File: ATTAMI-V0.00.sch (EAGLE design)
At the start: 23 parts, among them U1 MIC5225, U2 ATTINY85-20SU

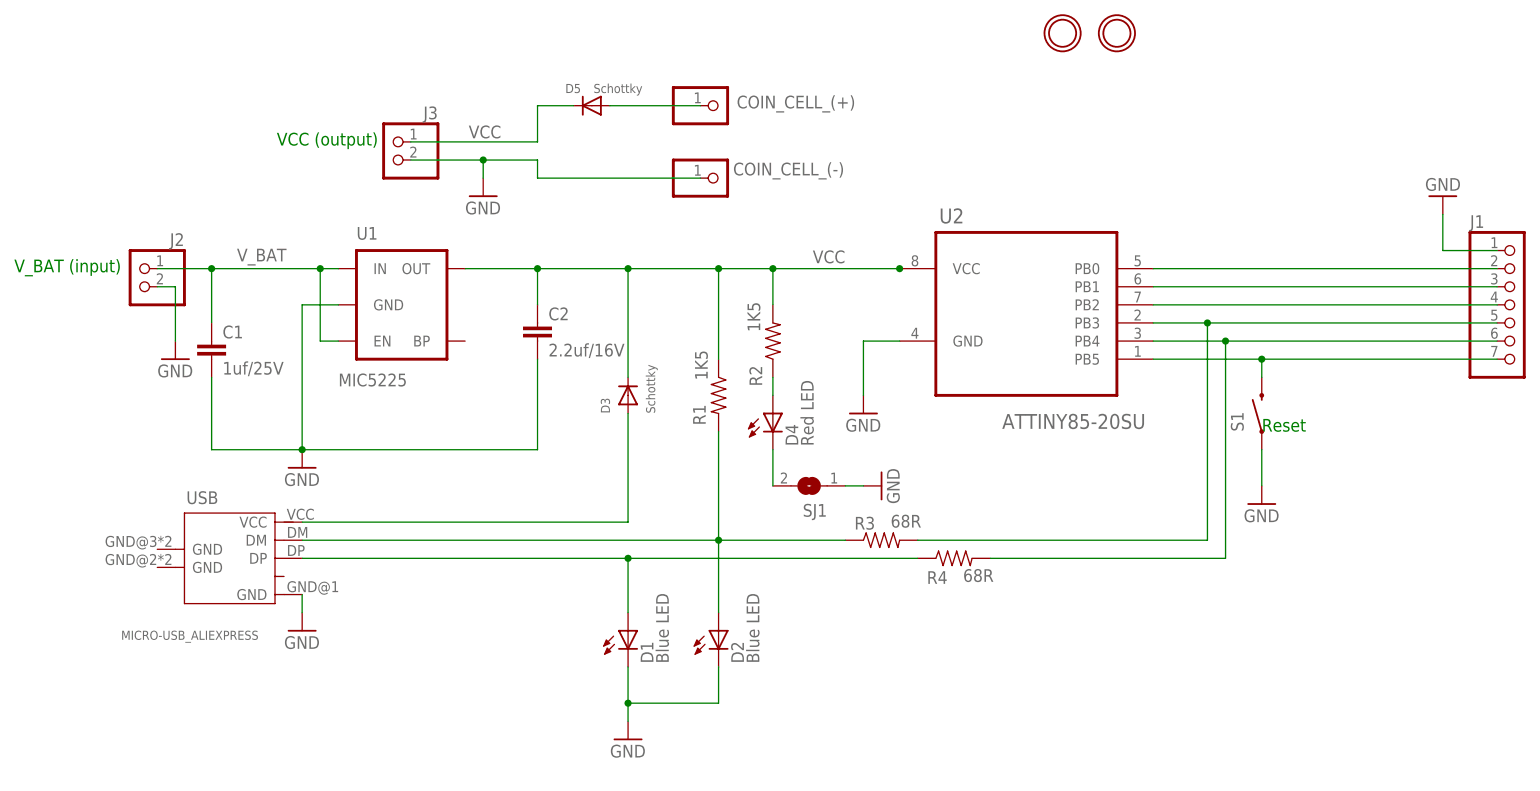
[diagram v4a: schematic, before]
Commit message: updated layout
including re-routing the EN-VIN connection on U1 and removing a few
routes that allows for this design to work as a one layer board with a
bit of work.
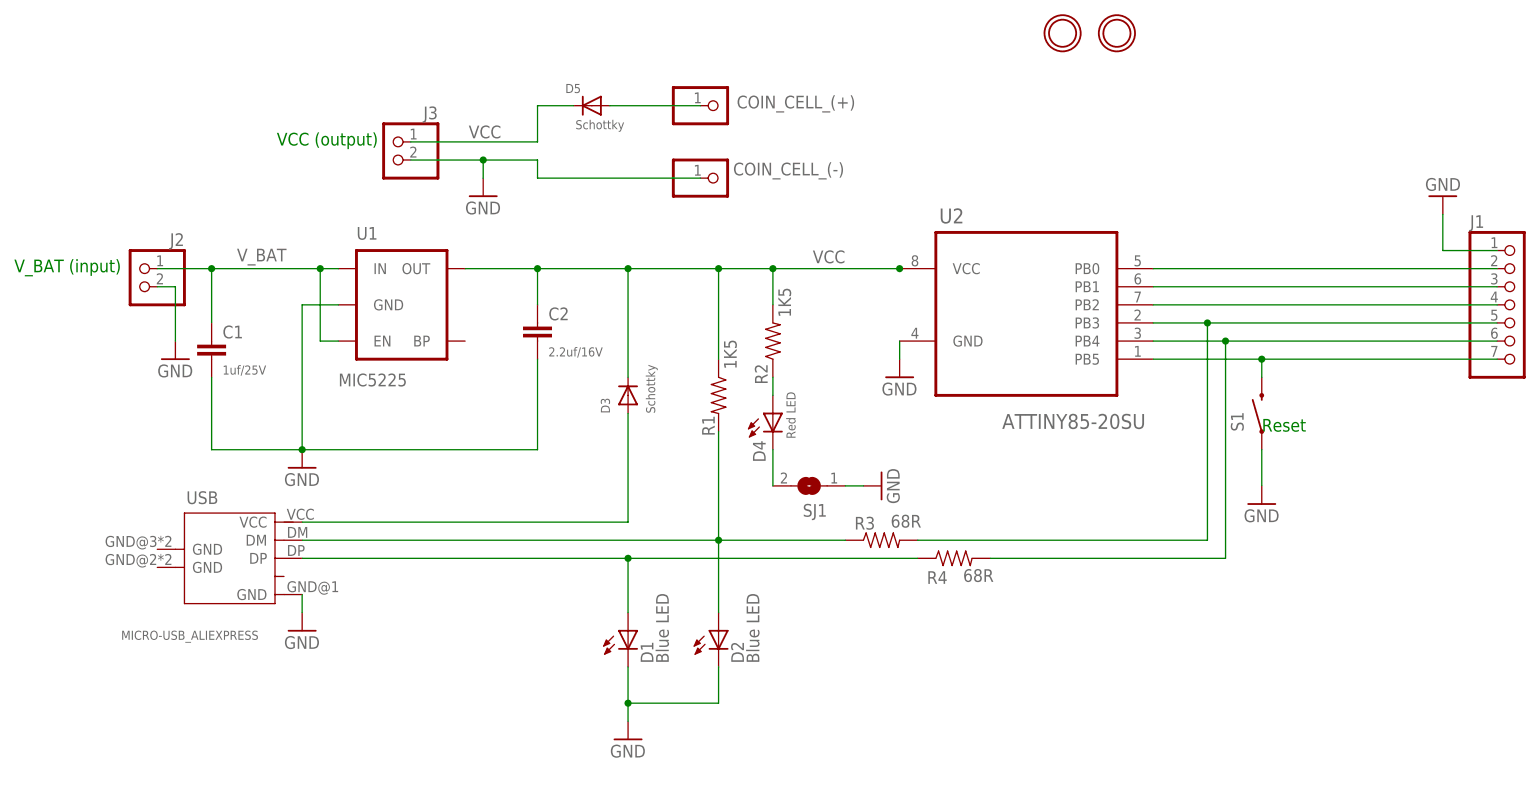
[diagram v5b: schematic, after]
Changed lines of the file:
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@@
 </instance>
 <instance part="R1" gate="G$1" x="121.92" y="109.22" smashed="yes" rot="R270">
-<attribute name="NAME" x="118.3386" y="107.95" size="1.778" layer="95" rot="R270"/>
-<attribute name="VALUE" x="118.618" y="115.57" size="1.778" layer="96" rot="R270"/>
+<attribute name="NAME" x="119.6086" y="106.426" size="1.778" layer="95" rot="R270"/>
+<attribute name="VALUE" x="122.682" y="117.094" size="1.778" layer="96" rot="R270"/>
 </instance>
-<instance part="GND2" gate="1" x="142.24" y="106.68"/>
+<instance part="GND2" gate="1" x="147.32" y="111.76"/>
 <instance part="GND3" gate="1" x="109.22" y="60.96"/>
 <instance part="D3" gate="G$1" x="109.22" y="109.22" rot="R90"/>
-<instance part="C2" gate="G$1" x="96.52" y="116.84"/>
+<instance part="C2" gate="G$1" x="96.52" y="116.84" smashed="yes">
+<attribute name="NAME" x="98.044" y="119.761" size="1.778" layer="95"/>
+<attribute name="VALUE" x="98.044" y="114.681" size="1.27" layer="96"/>
+</instance>
 <instance part="D1" gate="LED" x="109.22" y="76.2"/>
 <instance part="D2" gate="LED" x="121.92" y="76.2"/>
@@
 <instance part="C1" gate="G$1" x="50.8" y="114.3" smashed="yes">
 <attribute name="NAME" x="52.324" y="117.221" size="1.778" layer="95"/>
-<attribute name="VALUE" x="52.324" y="112.141" size="1.778" layer="96"/>
+<attribute name="VALUE" x="52.324" y="112.141" size="1.27" layer="96"/>
 </instance>
-<instance part="D4" gate="LED" x="129.54" y="106.68"/>
+<instance part="D4" gate="LED" x="129.54" y="106.68" smashed="yes">
+<attribute name="NAME" x="128.524" y="99.822" size="1.778" layer="95" rot="R90"/>
+<attribute name="VALUE" x="132.715" y="103.124" size="1.27" layer="96" rot="R90"/>
+</instance>
 <instance part="R2" gate="G$1" x="129.54" y="116.84" smashed="yes" rot="R90">
-<attribute name="NAME" x="128.0414" y="110.49" size="1.778" layer="95" rot="R90"/>
-<attribute name="VALUE" x="127.762" y="118.11" size="1.778" layer="96" rot="R90"/>
+<attribute name="NAME" x="128.8034" y="110.744" size="1.778" layer="95" rot="R90"/>
+<attribute name="VALUE" x="132.08" y="120.142" size="1.778" layer="96" rot="R90"/>
 </instance>
 <instance part="GND12" gate="1" x="144.78" y="96.52" rot="R90"/>
@@
 <instance part="D5" gate="G$1" x="104.14" y="149.86" smashed="yes" rot="R180">
 <attribute name="NAME" x="102.616" y="152.908" size="1.27" layer="95" rot="R180"/>
-<attribute name="VALUE" x="111.252" y="152.908" size="1.27" layer="96" rot="R180"/>
+<attribute name="VALUE" x="108.712" y="147.828" size="1.27" layer="96" rot="R180"/>
 </instance>
 <instance part="SJ1" gate="1" x="134.62" y="96.52" rot="R180"/>
@@
 </segment>
 <segment>
-<wire x1="142.24" y1="116.84" x2="142.24" y2="109.22" width="0.1524" layer="91"/>
+<wire x1="147.32" y1="116.84" x2="147.32" y2="114.3" width="0.1524" layer="91"/>
 <pinref part="GND2" gate="1" pin="GND"/>
 <pinref part="U2" gate="A" pin="GND"/>
-<wire x1="147.32" y1="116.84" x2="142.24" y2="116.84" width="0.1524" layer="91"/>
 </segment>
 <segment>

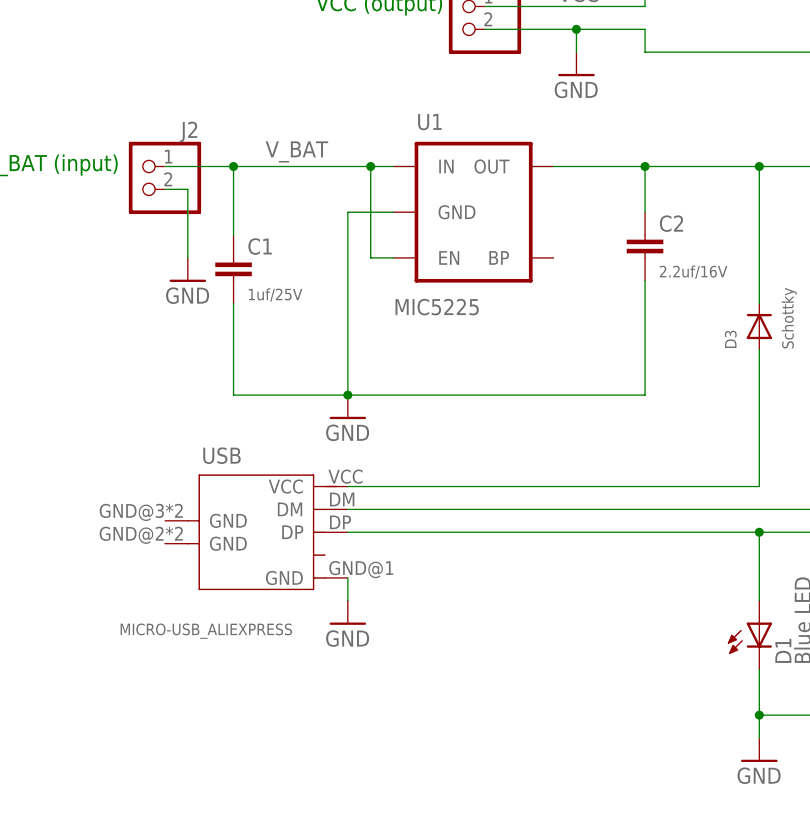
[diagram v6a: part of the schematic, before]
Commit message: new design with added AMS1117 voltage regulator
with library reflecting the part
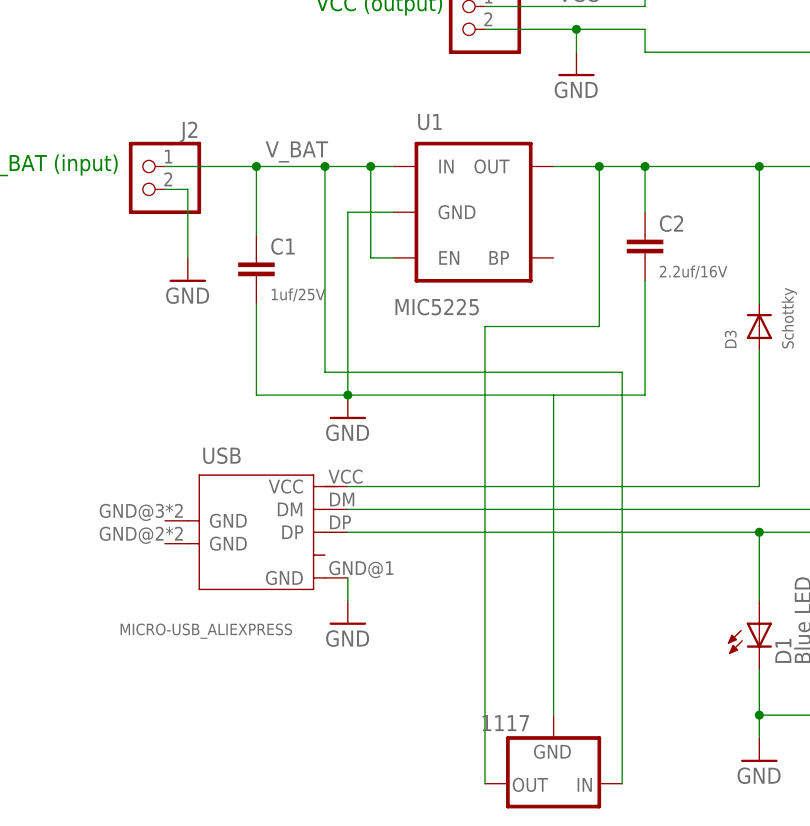
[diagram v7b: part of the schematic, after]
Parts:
- added 1117: (no value), ATtami:XXX1117-SOT89
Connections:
- net GND: now also 1117.GND
- net VCC: now also 1117.OUT
- net V_BAT: now also 1117.IN
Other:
- moved on the sheet: C1

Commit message: mostly lib work
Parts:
- added SJ2: (no value), microbuilder:SOLDERJUMPER_2WAY0603
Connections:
- new net N$1: R4.2, S1.2, SJ2.2
- net PB4: now also SJ2.3; no longer R4.2
- net PB5: now also SJ2.1; no longer S1.2
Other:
- note added: "midi jumper"
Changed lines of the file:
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@@
 <part name="U2" library="ATtami" deviceset="ATTINY85-20SU" device=""/>
 <part name="1117" library="ATtami" deviceset="XXX1117" device="-SOT89"/>
+<part name="SJ2" library="microbuilder" deviceset="SOLDERJUMPER_2WAY" device="0603"/>
 </parts>
 <sheets>
@@
 <text x="59.944" y="144.272" size="1.778" layer="91">VCC (output)</text>
 <text x="23.114" y="126.492" size="1.778" layer="91">V_BAT (input)</text>
-<text x="198.12" y="104.14" size="1.778" layer="91">Reset</text>
+<text x="204.978" y="94.996" size="1.778" layer="91" rot="R180">Reset</text>
+<text x="195.58" y="104.14" size="1.778" layer="91">midi jumper</text>
 </plain>
 <instances>
@@
 <instance part="D2" gate="LED" x="121.92" y="76.2"/>
 <instance part="GND16" gate="1" x="88.9" y="137.16"/>
-<instance part="GND13" gate="1" x="198.12" y="93.98"/>
+<instance part="GND13" gate="1" x="208.28" y="93.98"/>
 <instance part="GND1" gate="1" x="45.72" y="114.3"/>
 <instance part="GND6" gate="1" x="63.5" y="99.06" smashed="yes">
@@
 </instance>
 <instance part="U$1" gate="G$1" x="177.8" y="160.02"/>
-<instance part="S1" gate="G$1" x="198.12" y="106.68" smashed="yes" rot="R90">
-<attribute name="NAME" x="195.58" y="104.14" size="1.778" layer="95" rot="R90"/>
-</instance>
+<instance part="S1" gate="G$1" x="198.12" y="96.52" smashed="yes" rot="R180"/>
 <instance part="USB" gate="G$1" x="53.34" y="86.36" smashed="yes">
 <attribute name="NAME" x="47.244" y="93.98" size="1.778" layer="95" ratio="10"/>
@@
 </instance>
 <instance part="1117" gate="1" x="86.36" y="58.42" rot="R180"/>
+<instance part="SJ2" gate="G$1" x="193.04" y="106.68" smashed="yes" rot="R180">
+<attribute name="VALUE" x="198.12" y="113.03" size="1.778" layer="96" rot="R180"/>
+</instance>
 </instances>
 <busses>
@@
 <segment>
 <pinref part="GND13" gate="1" pin="GND"/>
-<wire x1="198.12" y1="101.6" x2="198.12" y2="96.52" width="0.1524" layer="91"/>
 <pinref part="S1" gate="G$1" pin="1"/>
+<wire x1="203.2" y1="96.52" x2="208.28" y2="96.52" width="0.1524" layer="91"/>
 </segment>
 <segment>
@@
 <net name="PB3" class="0">
 <segment>
-<wire x1="190.5" y1="88.9" x2="149.86" y2="88.9" width="0.1524" layer="91"/>
+<wire x1="185.42" y1="88.9" x2="149.86" y2="88.9" width="0.1524" layer="91"/>
 <pinref part="R3" gate="G$1" pin="2"/>
-<wire x1="182.88" y1="119.38" x2="190.5" y2="119.38" width="0.1524" layer="91"/>
-<wire x1="190.5" y1="119.38" x2="190.5" y2="88.9" width="0.1524" layer="91"/>
-<wire x1="190.5" y1="119.38" x2="231.14" y2="119.38" width="0.1524" layer="91"/>
-<junction x="190.5" y="119.38"/>
+<wire x1="182.88" y1="119.38" x2="185.42" y2="119.38" width="0.1524" layer="91"/>
+<wire x1="185.42" y1="119.38" x2="185.42" y2="88.9" width="0.1524" layer="91"/>
+<wire x1="185.42" y1="119.38" x2="231.14" y2="119.38" width="0.1524" layer="91"/>
+<junction x="185.42" y="119.38"/>
 <pinref part="J1" gate="A" pin="5"/>
 <pinref part="U2" gate="A" pin="PB3"/>
@@
 <net name="PB4" class="0">
 <segment>
-<pinref part="R4" gate="G$1" pin="2"/>
-<wire x1="160.02" y1="86.36" x2="193.04" y2="86.36" width="0.1524" layer="91"/>
-<wire x1="182.88" y1="116.84" x2="193.04" y2="116.84" width="0.1524" layer="91"/>
-<wire x1="193.04" y1="116.84" x2="193.04" y2="86.36" width="0.1524" layer="91"/>
-<wire x1="193.04" y1="116.84" x2="231.14" y2="116.84" width="0.1524" layer="91"/>
-<junction x="193.04" y="116.84"/>
+<wire x1="182.88" y1="116.84" x2="190.5" y2="116.84" width="0.1524" layer="91"/>
 <pinref part="J1" gate="A" pin="6"/>
 <pinref part="U2" gate="A" pin="PB4"/>
+<pinref part="SJ2" gate="G$1" pin="3"/>
+<wire x1="190.5" y1="116.84" x2="231.14" y2="116.84" width="0.1524" layer="91"/>
+<wire x1="190.5" y1="106.68" x2="190.5" y2="116.84" width="0.1524" layer="91"/>
+<junction x="190.5" y="116.84"/>
 </segment>
 </net>
 <net name="PB5" class="0">
 <segment>
-<pinref part="S1" gate="G$1" pin="2"/>
 <pinref part="J1" gate="A" pin="7"/>
-<wire x1="231.14" y1="114.3" x2="198.12" y2="114.3" width="0.1524" layer="91"/>
-<wire x1="198.12" y1="114.3" x2="198.12" y2="111.76" width="0.1524" layer="91"/>
-<wire x1="182.88" y1="114.3" x2="198.12" y2="114.3" width="0.1524" layer="91"/>
-<junction x="198.12" y="114.3"/>
+<wire x1="231.14" y1="114.3" x2="195.58" y2="114.3" width="0.1524" layer="91"/>
 <pinref part="U2" gate="A" pin="PB5"/>
+<wire x1="182.88" y1="114.3" x2="195.58" y2="114.3" width="0.1524" layer="91"/>
+<pinref part="SJ2" gate="G$1" pin="1"/>
+<wire x1="195.58" y1="114.3" x2="195.58" y2="106.68" width="0.1524" layer="91"/>
+<junction x="195.58" y="114.3"/>
 </segment>
 </net>
@@
 </segment>
 </net>
+<net name="N$1" class="0">
+<segment>
+<pinref part="R4" gate="G$1" pin="2"/>
+<wire x1="160.02" y1="86.36" x2="193.04" y2="86.36" width="0.1524" layer="91"/>
+<wire x1="193.04" y1="86.36" x2="193.04" y2="96.52" width="0.1524" layer="91"/>
+<pinref part="SJ2" gate="G$1" pin="2"/>
+<pinref part="S1" gate="G$1" pin="2"/>
+<wire x1="193.04" y1="96.52" x2="193.04" y2="104.14" width="0.1524" layer="91"/>
+<junction x="193.04" y="96.52"/>
+</segment>
+</net>
